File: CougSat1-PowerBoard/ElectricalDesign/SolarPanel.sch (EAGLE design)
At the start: 120 parts, among them J100 ADCS, J101 EPS, U1 INA199C2, U100 SPV1040, U101 SPV1040, U2 INA199C2, U3 INA199C2, U4 INA199C2, U5 AD7291, U6 AD7291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

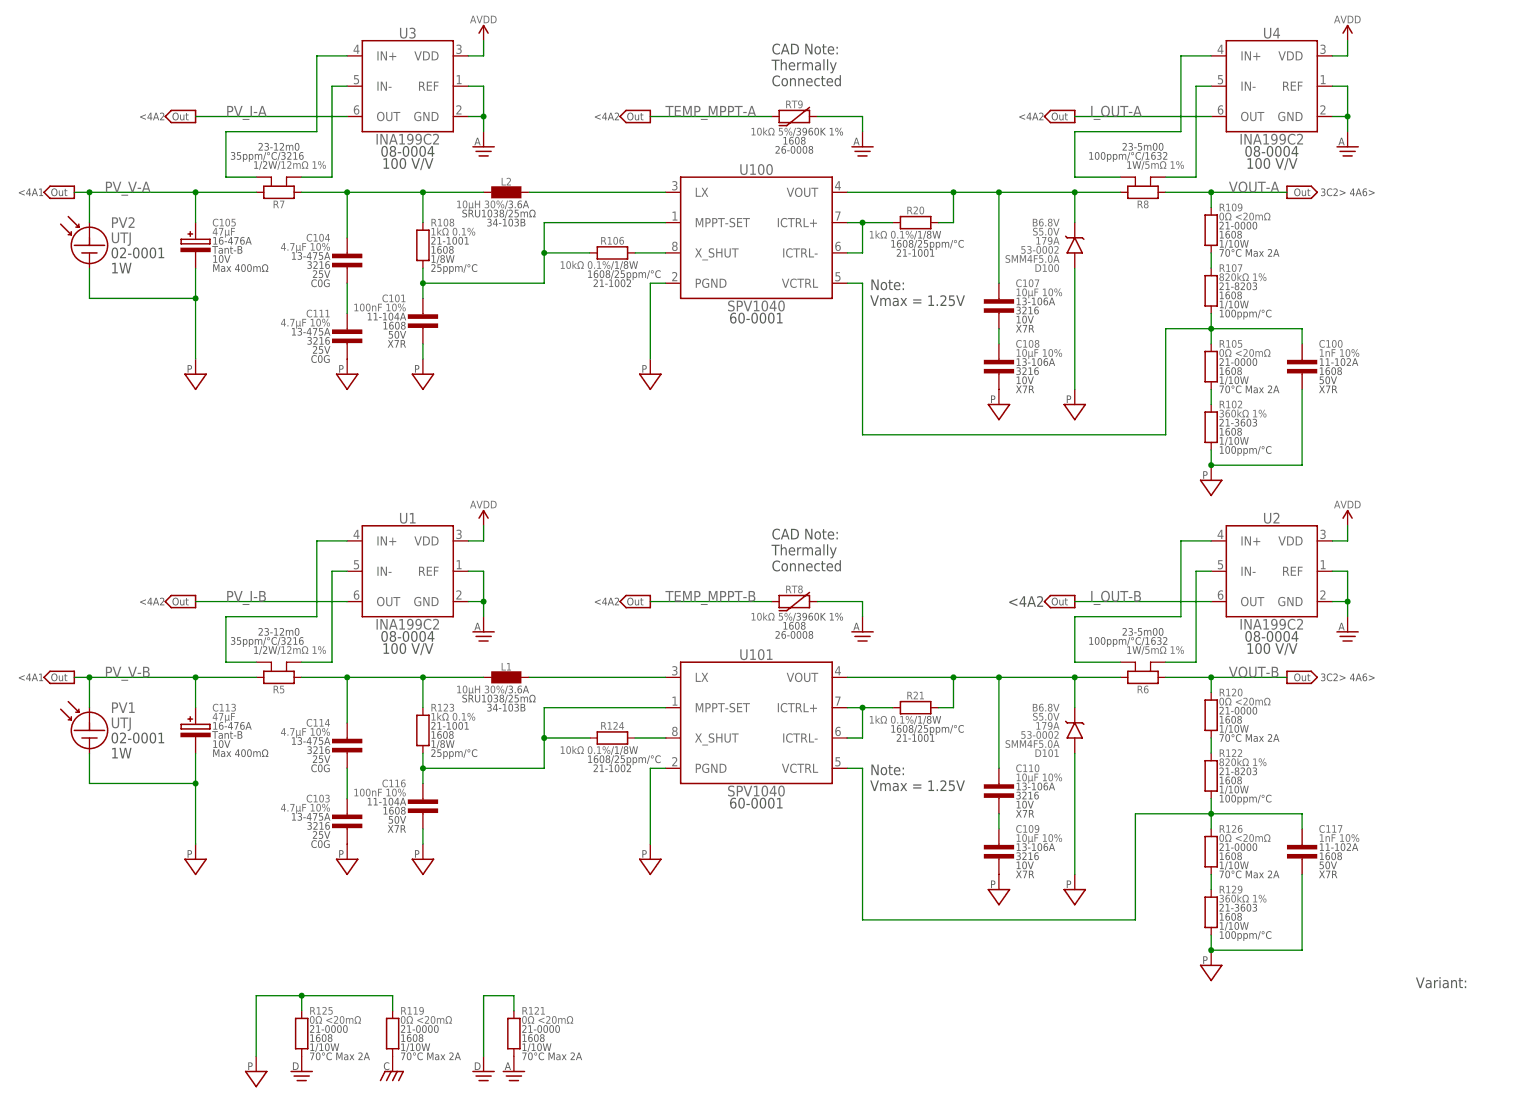
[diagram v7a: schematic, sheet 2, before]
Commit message: Placed most components for battery chargers
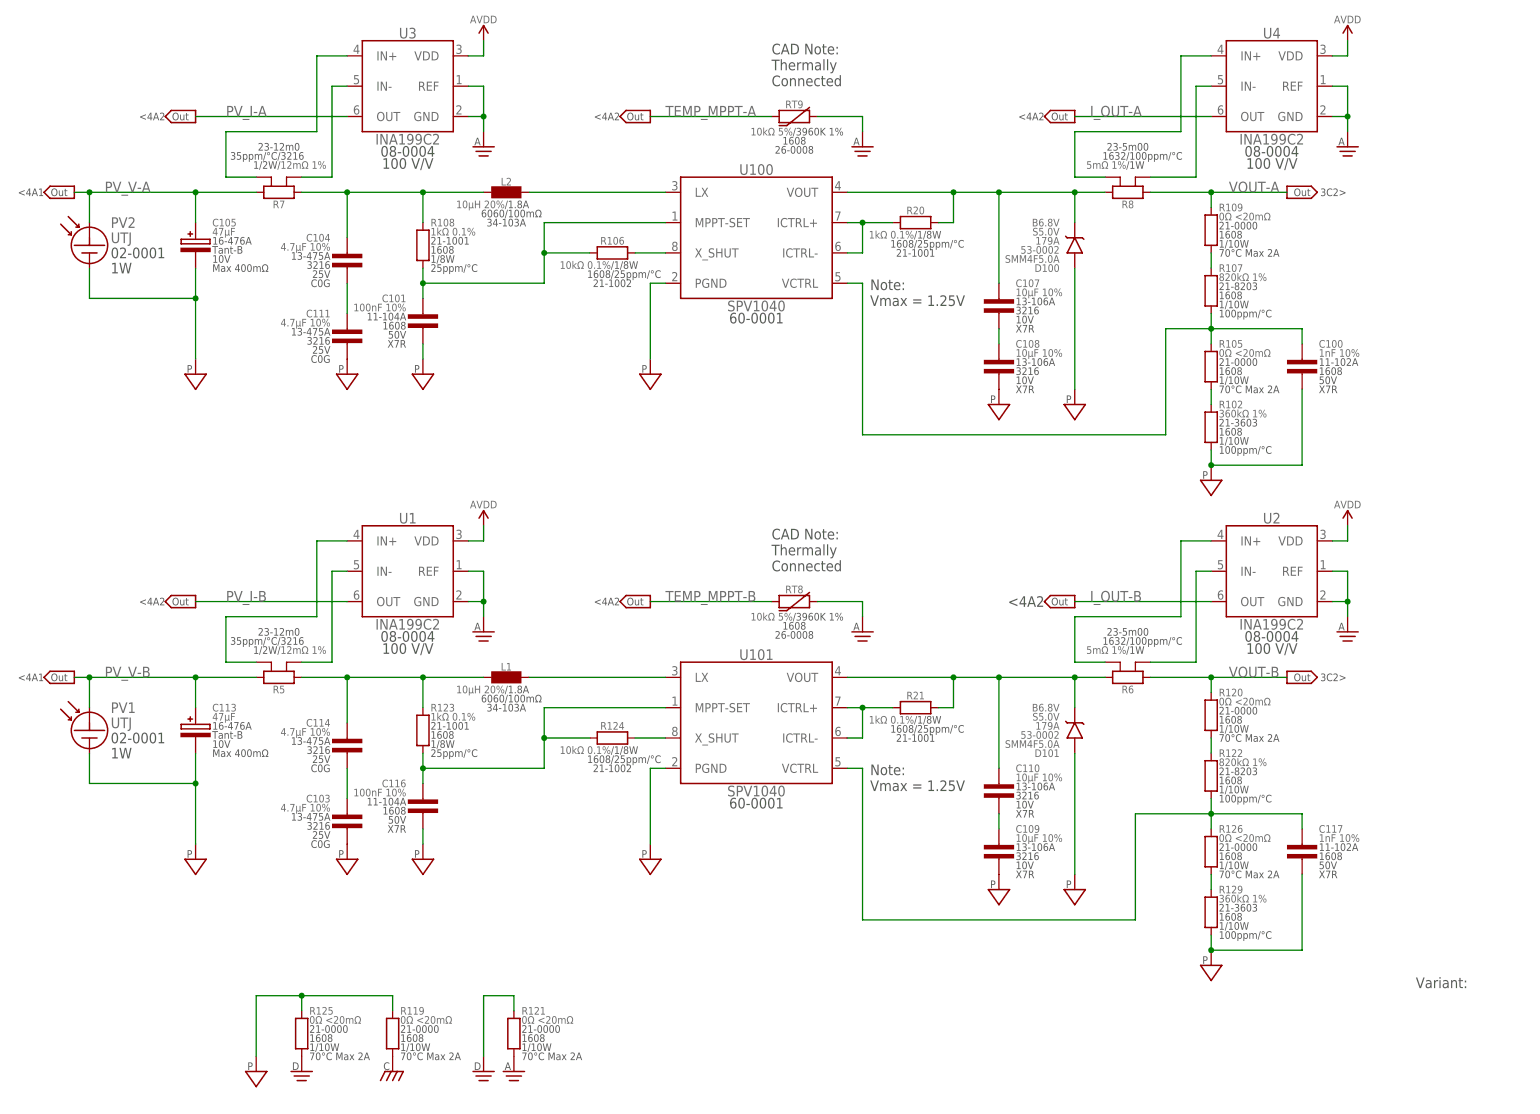
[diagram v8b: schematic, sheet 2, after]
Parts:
- L1, L2: value 10µH 30% -> 10µH 20%; device CougsInSpace-Coils:INDUCTOR-H-10UH-SRU1038 -> CougsInSpace-Coils:INDUCTOR-H-10UH-6060
- R17: value 1.33kΩ 0.1% -> 1.2kΩ 0.1%; device CougsInSpace-Resistors:RES-V-1.33K-1608 -> CougsInSpace-Resistors:RES-V-1.2K-1608
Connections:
- net MPPT_VOUT-A: now also R8.1; no longer R8.2
- net MPPT_VOUT-B: now also R6.1; no longer R6.2
- net VOUT-A: now also R8.2; no longer R8.1
- net VOUT-B: now also R6.2; no longer R6.1
- net VOUT_N-A: now also R8.2-KELVIN; no longer R8.1-KELVIN
- net VOUT_N-B: now also R6.2-KELVIN; no longer R6.1-KELVIN
- net VOUT_P-A: now also R8.1-KELVIN; no longer R8.2-KELVIN
- net VOUT_P-B: now also R6.1-KELVIN; no longer R6.2-KELVIN
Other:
- note added: "3C2>"
- note removed: "3C2> 4A6>"
- moved on the sheet: R6, R8
